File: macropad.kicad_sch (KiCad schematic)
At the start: 64 parts, among them J1 USB_C_Receptacle_USB2.0, J11 Conn_01x04_Pin, J3 Conn_01x03, J6 Conn_01x05_Pin, J7 Conn_01x04_Pin, J9 Conn_01x02_Pin, SW1 RotaryEncoder_Switch, SW2 SW_Push, SW3 SW_Push, SW4 SW_Push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

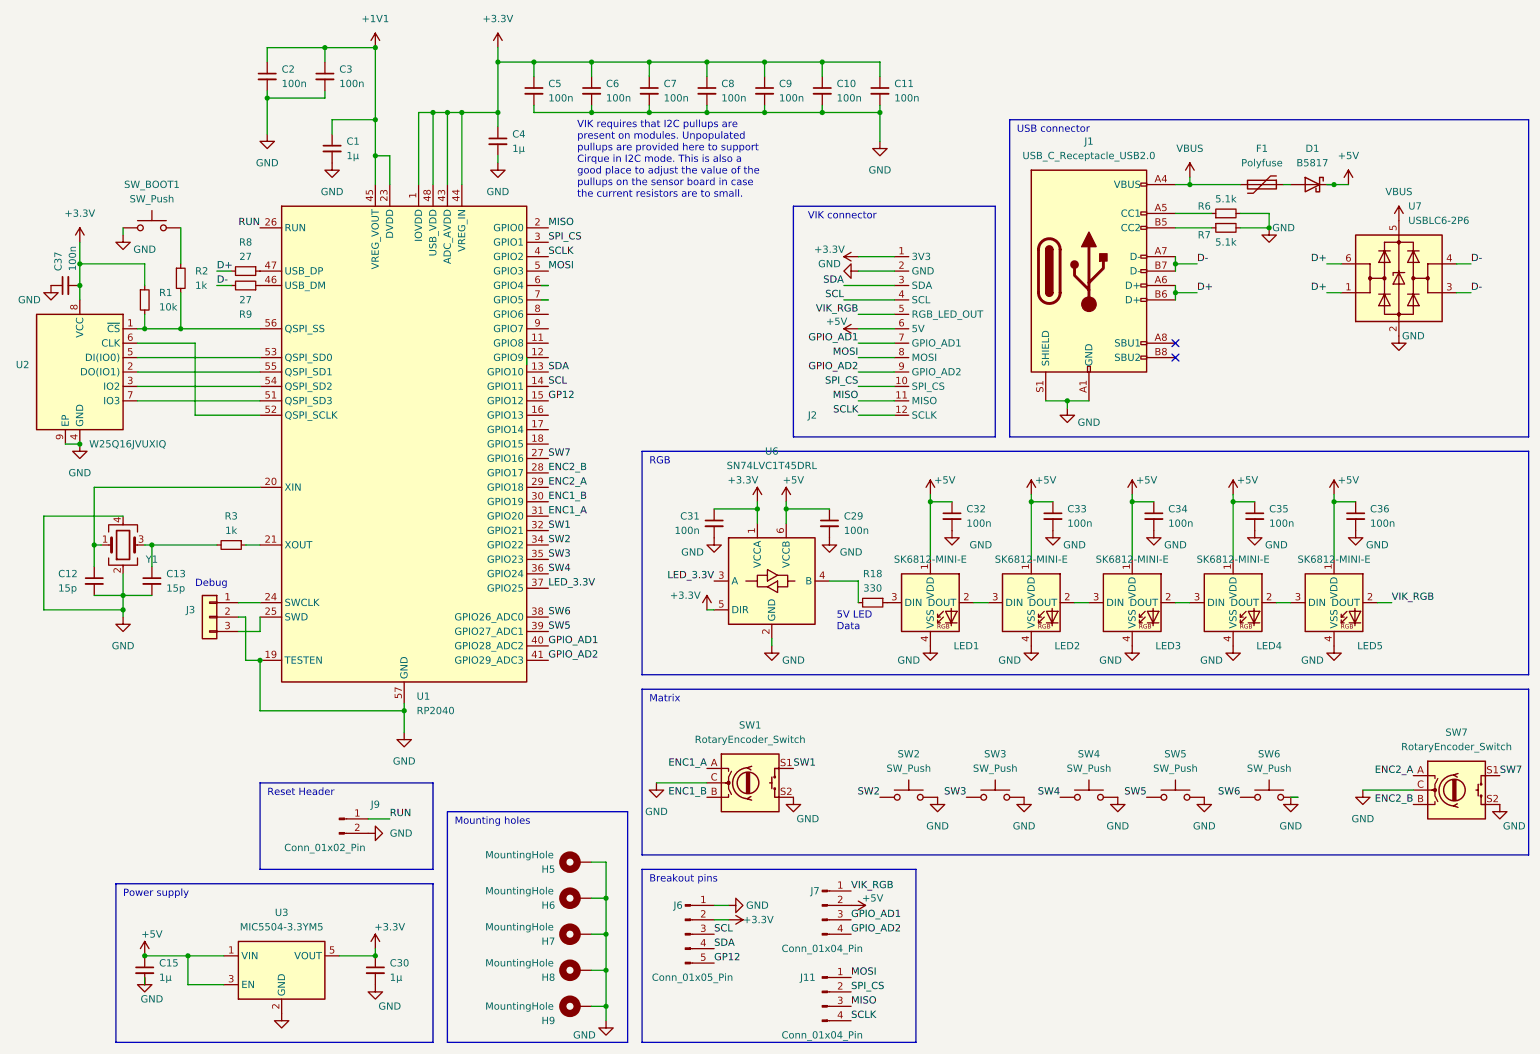
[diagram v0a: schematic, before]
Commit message: smashed everything into one PCB and removed some parts I don't want.
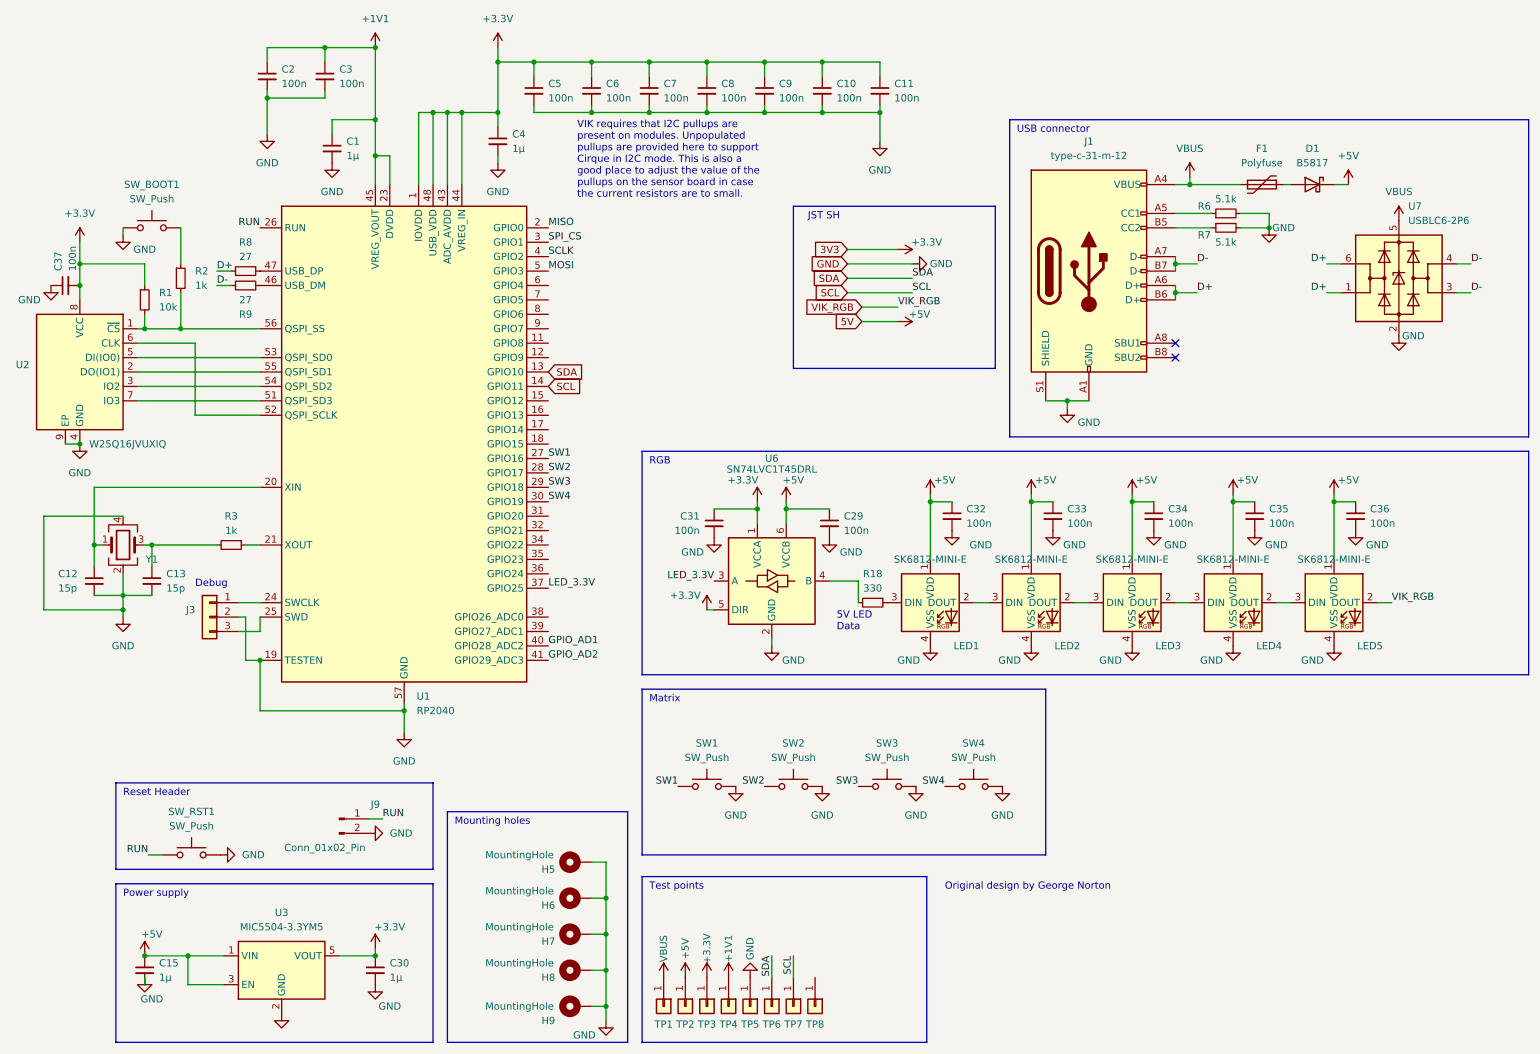
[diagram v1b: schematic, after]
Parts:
- removed J11: Conn_01x04_Pin, Connector_PinSocket_1.00mm:PinSocket_1x04_P1.00mm_Vertical, symbol Connector:Conn_01x04_Pin
- removed J2: ~, Vik:vik-keyboard-connector-horizontal, symbol Vik:vik-keyboard-connector
- removed J6: Conn_01x05_Pin, Connector_PinHeader_2.54mm:PinHeader_1x05_P2.54mm_Vertical, symbol Connector:Conn_01x05_Pin
- removed J7: Conn_01x04_Pin, Connector_PinHeader_2.54mm:PinHeader_1x04_P2.54mm_Vertical, symbol Connector:Conn_01x04_Pin
- removed SW1, SW7: RotaryEncoder_Switch, Trackpad:ROT_Alps_EC11E-Switch, symbol Device:RotaryEncoder_Switch
- removed SW6: SW_Push, PCM_marbastlib-xp-choc:SW_choc_MxCombo_1u, symbol Switch:SW_Push
- added SW_RST1: SW_Push, Button_Switch_SMD:SW_SPST_B3U-1000P, symbol Switch:SW_Push
- added TP1, TP2, TP3, TP4, TP5, TP6, TP7, TP8: TP, TestPoint:TestPoint_THTPad_D1.0mm_Drill0.5mm, symbol Connector_Generic:Conn_01x01
- J1: value USB_C_Receptacle_USB2.0 -> type-c-31-m-12
- J3: value Conn_01x03 -> JST 3P; footprint Connector_PinHeader_2.54mm:PinHeader_1x03_P2.54mm_Vertical -> Connector_JST:JST_SH_BM03B-SRSS-TB_1x03-1MP_P1.00mm_Vertical
- SW1: renamed from SW2; footprint PCM_marbastlib-xp-choc:SW_choc_MxCombo_1u -> Connector_PinHeader_1.00mm:PinHeader_1x02_P1.00mm_Vertical
- SW2: renamed from SW3; footprint PCM_marbastlib-xp-choc:SW_choc_MxCombo_1u -> Connector_PinHeader_1.00mm:PinHeader_1x02_P1.00mm_Vertical
- SW3: renamed from SW4; footprint PCM_marbastlib-xp-choc:SW_choc_MxCombo_1u -> Connector_PinHeader_1.00mm:PinHeader_1x02_P1.00mm_Vertical
- SW4: renamed from SW5; footprint PCM_marbastlib-xp-choc:SW_choc_MxCombo_1u -> Connector_PinHeader_1.00mm:PinHeader_1x02_P1.00mm_Vertical
- SW_BOOT1: footprint Button_Switch_SMD:SW_SPST_CK_KXT3 -> Button_Switch_SMD:SW_SPST_B3U-1000P
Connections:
- net ENC1_B is gone; now on net SW4: U1.30 (GPIO19)
- net ENC2_A is gone; now on net SW3: U1.29 (GPIO18)
- net ENC2_B is gone; now on net SW2: U1.28 (GPIO17)
- net SW7 is gone; now on net SW1: U1.27 (GPIO16)
- net +1V1: now also TP4.1 (Pin_1)
- net +3.3V: now also TP3.1 (Pin_1)
- net +5V: now also TP2.1 (Pin_1)
- net GND: now also SW_RST1.2, TP5.1 (Pin_1)
- net RUN: now also SW_RST1.1
- net SCL: now also TP7.1 (Pin_1)
- net SDA: now also TP6.1 (Pin_1)
- net SW1: now also SW1.2; no longer U1.32 (GPIO21)
- net SW2: now also SW2.2; no longer SW1.2, U1.34 (GPIO22)
- net SW3: now also SW3.2; no longer SW2.2, U1.35 (GPIO23)
- net SW4: now also SW4.2; no longer SW3.2, U1.36 (GPIO24)
- net VBUS: now also TP1.1 (Pin_1)
- net ENC1_A: no longer names the net of U1.31 (GPIO20)
- net GP12: no longer names the net of U1.15 (GPIO12)
- net SW5: no longer names the net of U1.39 (GPIO27_ADC1)
- net SW5: no longer SW4.2
- net SW6: no longer names the net of U1.38 (GPIO26_ADC0)
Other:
- note added: "JST SH"
- note added: "Original design by George Norton"
- note added: "Test points"
- note removed: "Breakout pins"
- note removed: "VIK connector"
- company: George Norton -> (none)
- moved on the sheet: SW1, SW2, SW3, SW4
